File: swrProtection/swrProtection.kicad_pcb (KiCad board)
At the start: 2 copper layers, 26 x 28 mm, 20 parts, among them J1 Conn_01x02, J2 Conn_01x02, J3 Conn_01x02, J4 Conn_01x02, J5 Conn_01x02, Q1 BSS123, U1 TLV4062/TLV4082, U2 74LVC2G00, U5 74LVC2G00

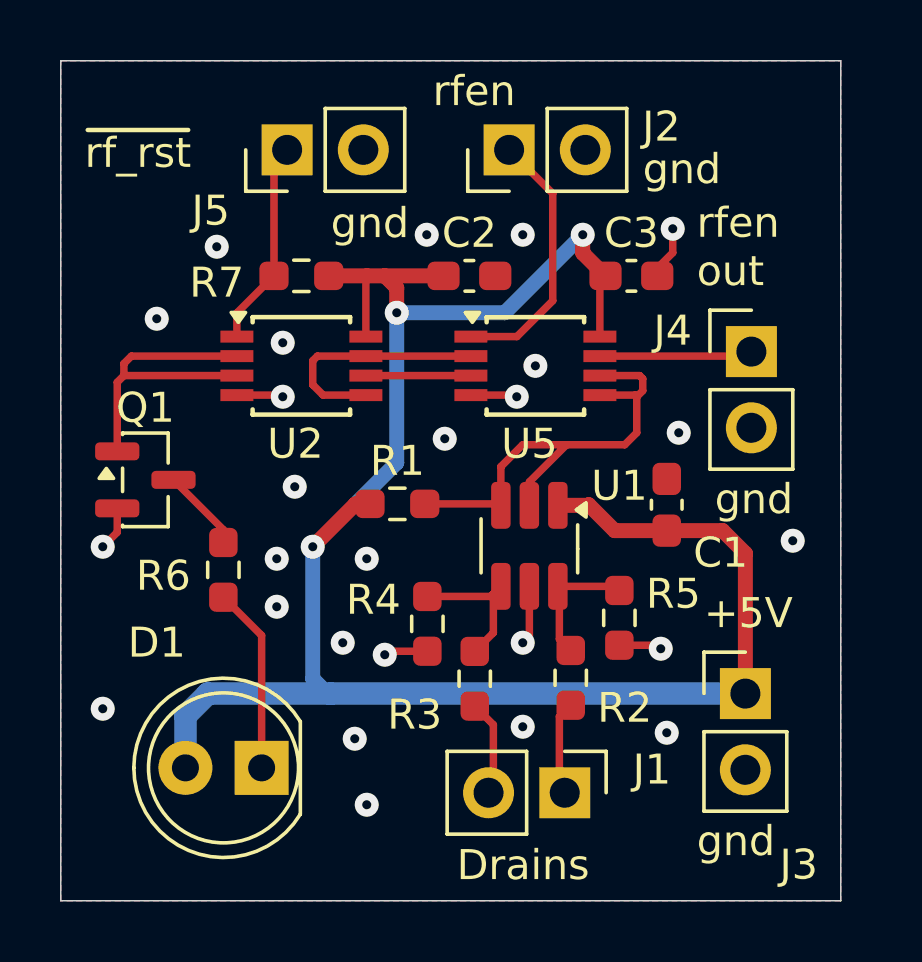
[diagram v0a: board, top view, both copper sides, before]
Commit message: updated swr schematic and board
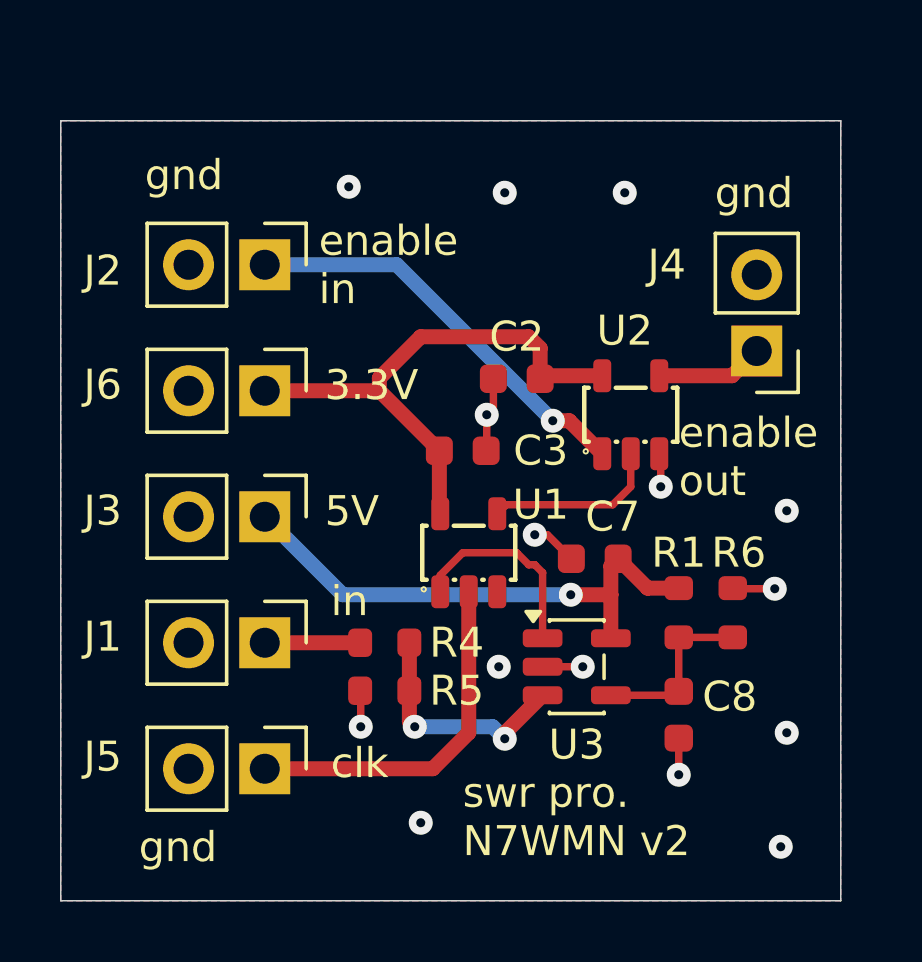
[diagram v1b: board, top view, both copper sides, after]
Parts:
- removed C1: 0.1uF, Capacitor_SMD:C_0603_1608Metric_Pad1.08x0.95mm_HandSolder
- removed D1: LED_Small, LED_THT:LED_D5.0mm
- removed Q1: BSS123, Package_TO_SOT_SMD:SOT-23
- removed R2, R3: 309k, Resistor_SMD:R_0603_1608Metric_Pad0.98x0.95mm_HandSolder
- removed R7: 3.3k, Resistor_SMD:R_0603_1608Metric_Pad0.98x0.95mm_HandSolder
- removed U5: 74LVC2G00, Package_SO:TSSOP-8_3x3mm_P0.65mm
- added C7: 100nF, PCM_JLCPCB:C_0603, F.Cu at (145.8, 96.6)
- added C8: 100nF, PCM_JLCPCB:C_0603, F.Cu at (148.6, 101.8)
- added J6: Conn_01x02, Connector_PinHeader_2.54mm:PinHeader_1x02_P2.54mm_Vertical, F.Cu at (134.8, 91.0)
- added U3: TLV7031DBV, Package_TO_SOT_SMD:SOT-23-5, F.Cu at (145.2, 100.2)
- C2, C3: value 0.1uF -> 100nF; footprint Capacitor_SMD:C_0603_1608Metric_Pad1.08x0.95mm_HandSolder -> PCM_JLCPCB:C_0603
- R1: value 3.3k -> 47kΩ; footprint Resistor_SMD:R_0603_1608Metric_Pad0.98x0.95mm_HandSolder -> PCM_JLCPCB:R_0603
- R4: value 4.7k -> 150kΩ; footprint Resistor_SMD:R_0603_1608Metric_Pad0.98x0.95mm_HandSolder -> PCM_JLCPCB:R_0603
- R5: value 4.7k -> 4.3kΩ; footprint Resistor_SMD:R_0603_1608Metric_Pad0.98x0.95mm_HandSolder -> PCM_JLCPCB:R_0603
- R6: value 560 -> 47kΩ; footprint Resistor_SMD:R_0603_1608Metric_Pad0.98x0.95mm_HandSolder -> PCM_JLCPCB:R_0603
- U1: value TLV4062/TLV4082 -> 74LVC1G79; footprint Package_TO_SOT_SMD:SOT-23-6_Handsoldering -> PCM_JLCPCB:SOT-23-5_L3.0-W1.7-P0.95-LS2.8-BR
- U2: value 74LVC2G00 -> 74AHCT1G32; footprint Package_SO:TSSOP-8_3x3mm_P0.65mm -> PCM_JLCPCB:SOT-23-5_L3.0-W1.7-P0.95-LS2.8-BR
- moved J5 20.6 mm to (134.8, 103.6), turned to -90 degrees
- moved J3 17.1 mm to (134.8, 95.2), turned to -90 degrees
- moved R6 17.0 mm to (150.4, 98.4)
- moved J1 11.2 mm to (134.8, 99.4)
- moved U2 11.1 mm to (147.0, 91.8), turned to -90 degrees
- moved R1 10.1 mm to (148.6, 98.4), turned to -90 degrees
- moved J2 9.00 mm to (134.8, 86.8), turned to -90 degrees
- moved R5 8.19 mm to (138.8, 101.0), turned to 180 degrees
- moved C3 8.10 mm to (141.4, 93.0)
- moved C2 3.78 mm to (143.2, 90.6), turned to 180 degrees
- moved U1 2.03 mm to (141.6, 96.4)
- moved R4 1.55 mm to (138.8, 99.4), turned to 0 degrees
- moved J4 0.18 mm to (151.2, 89.7), turned to 180 degrees
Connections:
- C2 pad 1: /VDD5 -> /VDD3p3
- C3 pad 1: /VDD5 -> /VDD3p3
- J1 pad 2: Net-(J1-Pin_2) -> GND
- J4 pad 1: /rf_enable_out -> /~{rf_enable_out}
- J5 pad 1: /~{rf_reset} -> /clock
- R1 pad 2: Net-(U1-OUT1) -> Net-(U3--)
- R4 pad 1: Net-(U1-IN2) -> Net-(J1-Pin_1)
- R4 pad 2: GND -> Net-(U3-+)
- R5 pad 1: Net-(U1-IN1) -> Net-(U3-+)
- R6 pad 1: Net-(D1-K) -> Net-(U3--)
- R6 pad 2: Net-(Q1-D) -> GND
- U1 pad 1: /VDD5 -> Net-(U1-D)
- U1 pad 2: Net-(U1-OUT1) -> /clock
- U1 pad 3: Net-(U1-OUT1) -> GND
- U1 pad 4: Net-(U1-IN2) -> Net-(U1-Q)
- U1 pad 5: GND -> /VDD3p3
- U2 pad 1: /~{rf_reset} -> /rf_enable
- U2 pad 2: Net-(Q1-G) -> Net-(U1-Q)
- U2 pad 3: Net-(Q1-G) -> GND
- U2 pad 4: GND -> /~{rf_enable_out}
- U2 pad 5: Net-(U2-Pad5) -> /VDD3p3
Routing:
- net /VDD5: track 67.3 -> 17.8 mm, vias 3 -> 1
- net /VDD3p3: track 0.00 -> 18.4 mm
- net Net-(U1-OUT1): track 16.0 -> 0.00 mm
- net /clock: track 0.00 -> 12.0 mm
- net Net-(Q1-G): track 10.7 -> 0.00 mm
- net Net-(U2-Pad5): track 8.05 -> 0.00 mm
- net Net-(U3-+): track 0.00 -> 8.01 mm, vias 0 -> 2
- net /~{rf_reset}: track 6.92 -> 0.00 mm
- net Net-(U1-D): track 0.00 -> 6.74 mm
- net Net-(D1-K): track 6.22 -> 0.00 mm
- net Net-(U1-Q): track 0.00 -> 5.92 mm
- net Net-(U3--): track 0.00 -> 5.92 mm
- net Net-(U1-IN2): track 5.12 -> 0.00 mm
- net /rf_enable_out: track 5.11 -> 0.00 mm
- net /rf_enable: track 8.86 -> 13.9 mm, vias 0 -> 1
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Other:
- board size 26 x 28 mm -> 26 x 26 mm
- board text added: "3.3V"
- board text added: "5V"
- board text added: "clk"
- board text added: "enable in"
- board text added: "enable out"
- board text added: "in"
- board text added: "swr pro. N7WMN v2"
- board text removed: "+5V"
- board text removed: "Drains"
- board text removed: "SWR Protection V1.0 N7WMN"
- board text removed: "rfen"
- board text removed: "rfen out"
- board text removed: "~{rf_rst}"

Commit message: swr protection final
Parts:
- removed U1: 74LVC1G79, PCM_JLCPCB:SOT-23-5_L3.0-W1.7-P0.95-LS2.8-BR
- removed U2: 74AHCT1G32, PCM_JLCPCB:SOT-23-5_L3.0-W1.7-P0.95-LS2.8-BR
- added J7: Conn_01x01, Connector_PinHeader_2.54mm:PinHeader_1x01_P2.54mm_Vertical, F.Cu at (152.0, 94.6)
- added R2: 47kΩ, PCM_JLCPCB:R_0603, F.Cu at (137.8, 94.4)
- added R3: 47kΩ, PCM_JLCPCB:R_0603, F.Cu at (148.2, 89.4)
- added U4: 74HCT74, Package_SO:SO-14_3.9x8.65mm_P1.27mm, F.Cu at (143.0, 92.4)
- added U5: 74LVC1G32, Package_TO_SOT_SMD:SOT-23-5, F.Cu at (140.6, 85.4)
- moved C3 9.54 mm to (146.6, 85.0), turned to 90 degrees
- moved C2 5.49 mm to (144.2, 85.2), turned to -90 degrees
- moved C7 2.43 mm to (145.4, 99.0)
- moved U3 1.41 mm to (145.4, 101.6)
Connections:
- C3 pad 1: /VDD3p3 -> /VDD5
- J2 pad 1: /rf_enable -> /~{rf_enable}
- J5 pad 1: /clock -> /tx_enable
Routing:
- net /tx_enable: track 0.00 -> 27.3 mm
- net /VDD5: track 17.8 -> 37.4 mm
- net /rf_enable: track 13.9 -> 0.00 mm, vias 1 -> 0
- net Net-(U4A-Q): track 0.00 -> 13.3 mm, vias 0 -> 2
- net Net-(J7-Pin_1): track 0.00 -> 12.2 mm, vias 0 -> 1
- net /clock: track 12.0 -> 0.00 mm
- net Net-(U4A-D): track 0.00 -> 7.65 mm
- net /~{rf_enable_out}: track 3.59 -> 10.8 mm, vias 0 -> 1
- net /~{rf_enable}: track 0.00 -> 6.57 mm
- net Net-(U1-Q): track 5.92 -> 0.00 mm
- net Net-(U4A-C): track 6.74 -> 12.5 mm
- net Net-(U4B-~{S}): track 0.00 -> 5.21 mm
- net GND: track 10.3 -> 5.17 mm, vias 15 -> 12
- net /VDD3p3: track 18.4 -> 17.9 mm, vias 0 -> 1
- net Net-(U3-+): track 8.01 -> 7.60 mm, vias 2 -> 0
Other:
- board text added: "en out"
- board text added: "rf en"
- board text added: "tx en"
- board text removed: "clk"
- board text removed: "enable in"
- board text removed: "enable out"
